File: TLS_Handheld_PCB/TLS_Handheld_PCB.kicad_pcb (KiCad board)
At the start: 4 copper layers, 175 x 100 mm, 95 parts, among them J1 Conn_01x02_Pin, J2 Conn_01x02_Pin, J3 Conn_01x02_Pin, M1 TO-236AB_SOT23_NEX, M2 TO-236AB_SOT23_NEX, U1 LT8640SEV_PBF, U2 LT8640SEV_PBF, U3 LT8619EDD-TRPBF, U4 LAA108STR, U5 SOP65P640X110-14N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

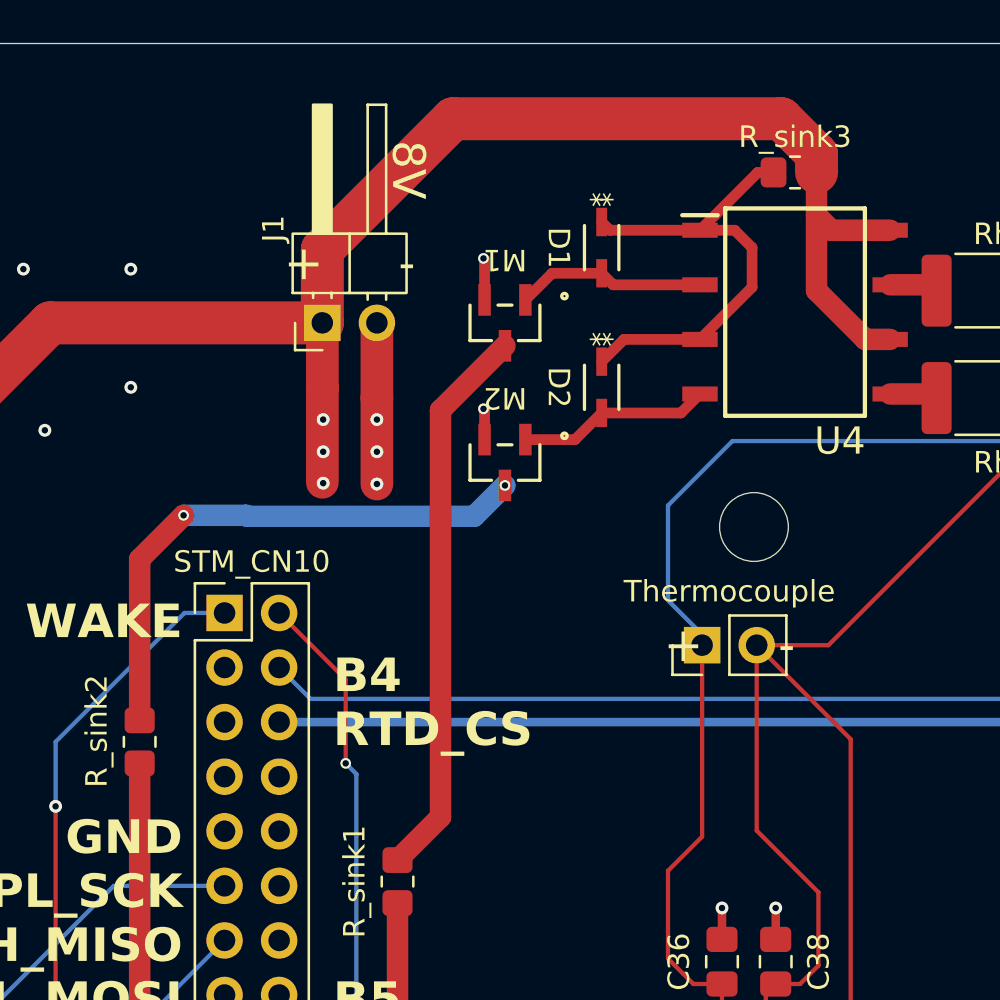
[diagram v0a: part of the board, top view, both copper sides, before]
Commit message: Update relay switching.
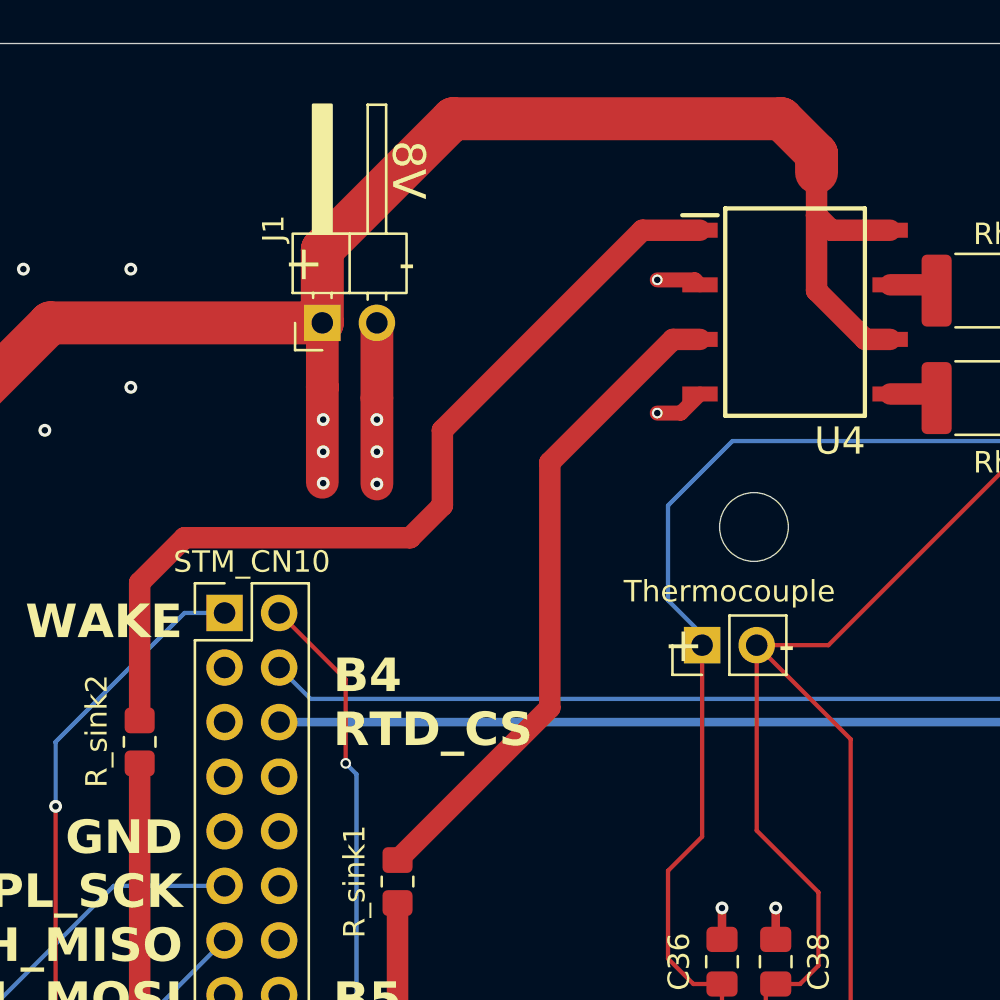
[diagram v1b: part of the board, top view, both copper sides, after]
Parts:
- removed D1, D2: CR_SOD-323_2L_ONS, Library:BAT54HT1G
- removed M1, M2: TO-236AB_SOT23_NEX, Library:2N7002NXAKR
- removed R_sink3: R_0805_2012Metric_Pad1.20x1.40mm_HandSolder, Resistor_SMD:R_0805_2012Metric_Pad1.20x1.40mm_HandSolder
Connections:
- R_sink1 pad 2: MOSFETGait2 -> SW2
- R_sink2 pad 2: MOSFETGait1 -> SW1
- U4 pad 1: SSRin+ -> SW1
- U4 pad 2: SSRin-1 -> GND
- U4 pad 3: SSRin+ -> SW2
- U4 pad 4: SSRin-2 -> GND
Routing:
- net SW1: track 0.00 -> 41.3 mm
- net SW2: track 0.00 -> 30.8 mm
- net MOSFETGait2: track 26.0 -> 0.00 mm
- net MOSFETGait1: track 26.0 -> 0.00 mm, vias 2 -> 0
- net SSRin+: track 22.3 -> 0.00 mm
- net SSRin-2: track 9.00 -> 0.00 mm
- net SSRin-1: track 8.86 -> 0.00 mm
- net GND: track 140.4 -> 141.5 mm

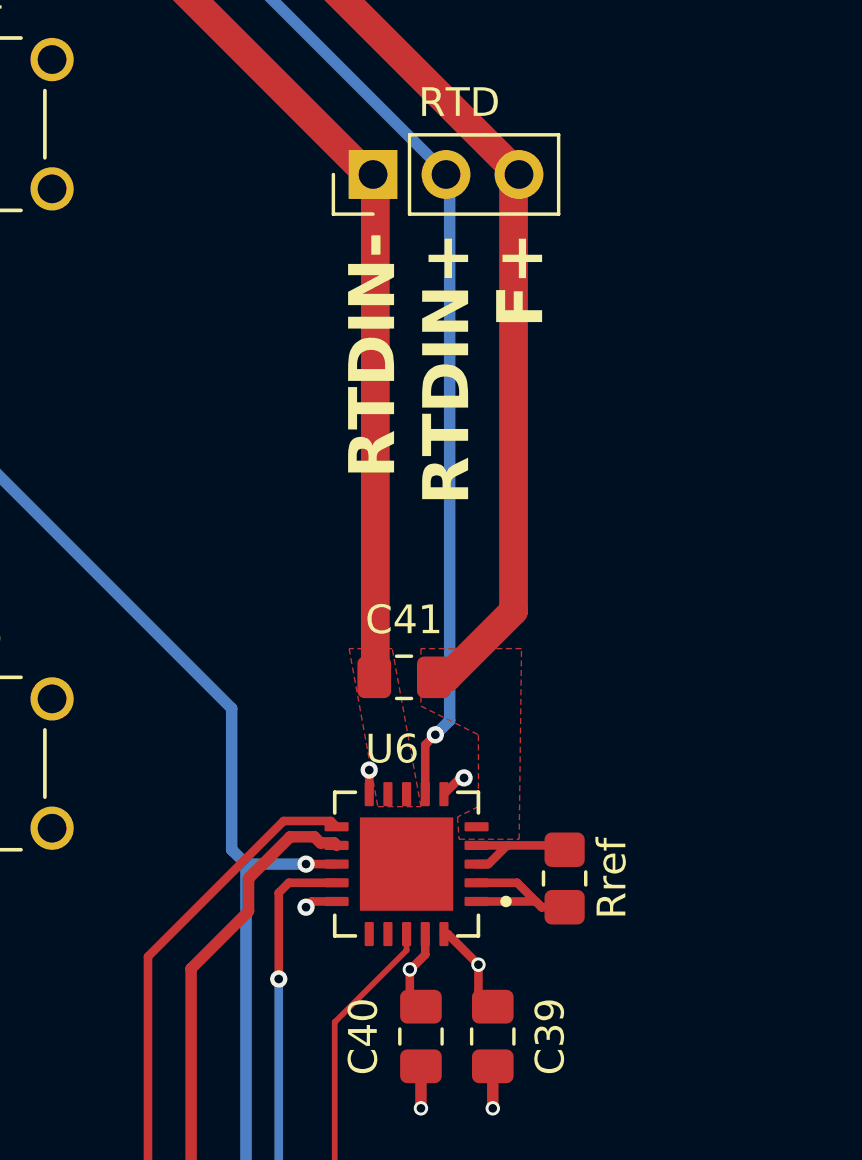
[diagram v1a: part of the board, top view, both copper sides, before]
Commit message: update rtd module wiring.
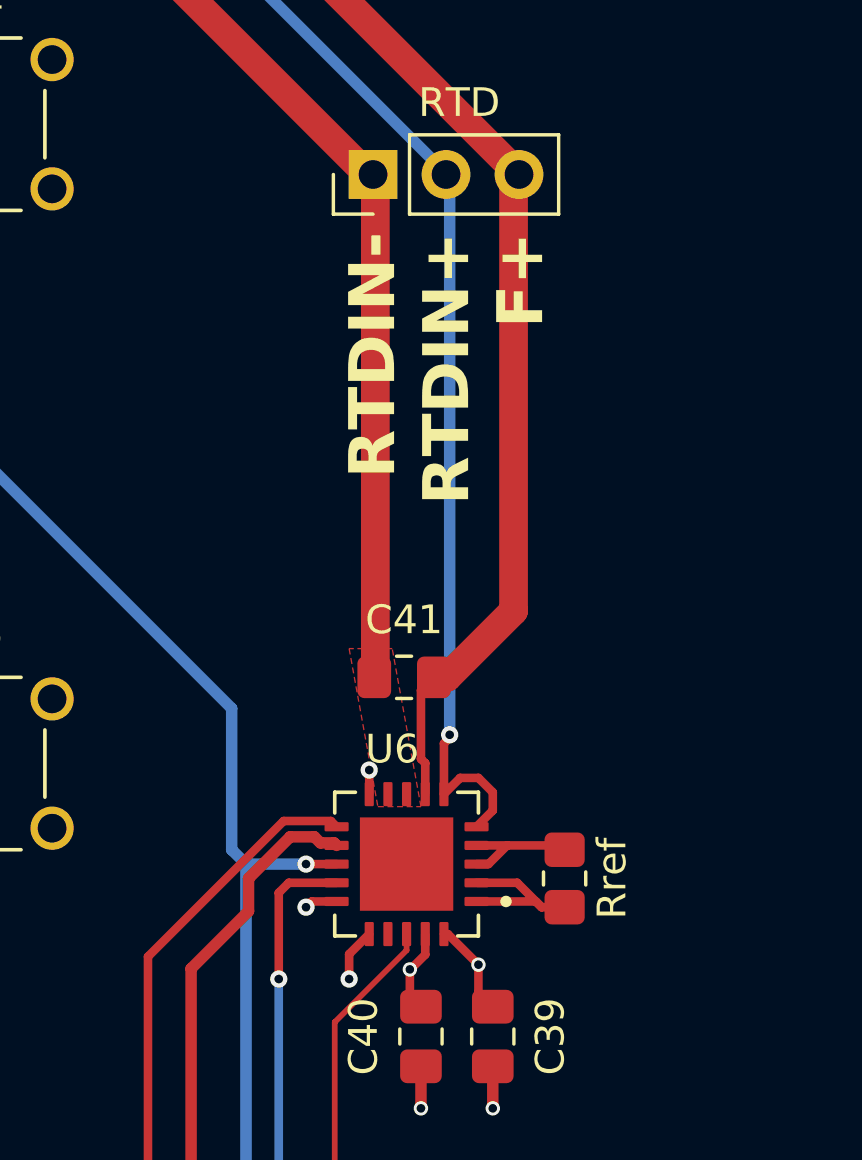
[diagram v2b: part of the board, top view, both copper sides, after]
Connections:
- U6 pad 16: (no net) -> GND
- U6 pad 5: RTD+ -> RTDSens
- U6 pad 6: GND -> RTDSens
- U6 pad 7: RTDSens -> RTD+
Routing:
- net RTD+: track 38.1 -> 42.4 mm
- net RTDSens: track 38.9 -> 42.2 mm
- net GND: track 141.5 -> 142.4 mm
- removed copper zone on F.Cu, net RTD+
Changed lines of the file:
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@@
 			(layers "F.Cu" "F.Mask" "F.Paste")
 			(roundrect_rratio 0.125)
-			(net 31 "RTD+")
+			(net 33 "RTDSens")
 			(solder_mask_margin 0.102)
 		)
@@
 			(layers "F.Cu" "F.Mask" "F.Paste")
 			(roundrect_rratio 0.125)
-			(net 1 "GND")
+			(net 33 "RTDSens")
 			(solder_mask_margin 0.102)
 		)
@@
 			(layers "F.Cu" "F.Mask" "F.Paste")
 			(roundrect_rratio 0.125)
-			(net 33 "RTDSens")
+			(net 31 "RTD+")
 			(solder_mask_margin 0.102)
 		)
@@
 			(layers "F.Cu" "F.Mask" "F.Paste")
 			(roundrect_rratio 0.125)
+			(net 1 "GND")
 			(solder_mask_margin 0.102)
 		)
@@
 	)
 	(segment
+		(start 223.2 94.935)
+		(end 222.5 95.635)
+		(width 0.3)
+		(layer "F.Cu")
+		(net 1)
+	)
+	(segment
 		(start 97.9125 124.5)
 		(end 100.6625 124.5)
@@
 	)
 	(segment
+		(start 222.5 95.635)
+		(end 222.5 96.5)
+		(width 0.3)
+		(layer "F.Cu")
+		(net 1)
+	)
+	(segment
 		(start 140.797 87)
 		(end 141.297 86.5)
@@
 	)
 	(segment
-		(start 226.365 89.5)
-		(end 226.5 89.5)
-		(width 0.3)
-		(layer "F.Cu")
-		(net 1)
-	)
-	(segment
 		(start 133.4195 122.5975)
 		(end 134.4595 121.5575)
@@
 	)
 	(segment
-		(start 225.8 90.065)
-		(end 226.365 89.5)
-		(width 0.3)
-		(layer "F.Cu")
-		(net 1)
-	)
-	(segment
 		(start 128.5 95)
 		(end 128.4266 95.0734)
@@
 	)
 	(via
-		(at 226.5 89.5)
-		(size 0.6)
-		(drill 0.3)
-		(layers "F.Cu" "B.Cu")
-		(net 1)
-	)
-	(via
 		(at 130.709499 55.6978)
 		(size 0.6)
@@
 	)
 	(via
+		(at 222.5 96.5)
+		(size 0.6)
+		(drill 0.3)
+		(layers "F.Cu" "B.Cu")
+		(net 1)
+	)
+	(via
 		(at 132.081242 86.064443)
 		(size 0.6)
@@
 	)
 	(segment
+		(start 225 86.45)
+		(end 225.45 86)
+		(width 0.3)
+		(layer "F.Cu")
+		(net 31)
+	)
+	(segment
+		(start 225.15 88.98781)
+		(end 225 88.83781)
+		(width 0.3)
+		(layer "F.Cu")
+		(net 31)
+	)
+	(segment
 		(start 215.572901 55.660401)
 		(end 228.2225 68.31)
@@
 	)
 	(segment
+		(start 225.15 90.065)
+		(end 225.15 88.98781)
+		(width 0.3)
+		(layer "F.Cu")
+		(net 31)
+	)
+	(segment
+		(start 225 88.83781)
+		(end 225 86.45)
+		(width 0.3)
+		(layer "F.Cu")
+		(net 31)
+	)
+	(segment
 		(start 226.935 92.5)
 		(end 227.35 92.5)
@@
 	)
 	(segment
-		(start 225.5 88)
-		(end 225.15 88.35)
+		(start 226.365 89.5)
+		(end 227 89.5)
 		(width 0.3)
 		(layer "F.Cu")
@@
 	)
 	(segment
-		(start 225.15 88.35)
-		(end 225.15 90.065)
+		(start 227 89.5)
+		(end 227.5 90)
+		(width 0.3)
+		(layer "F.Cu")
+		(net 33)
+	)
+	(segment
+		(start 226 88)
+		(end 226 88.1)
+		(width 0.3)
+		(layer "F.Cu")
+		(net 33)
+	)
+	(segment
+		(start 225.8 90.065)
+		(end 226.365 89.5)
+		(width 0.3)
+		(layer "F.Cu")
+		(net 33)
+	)
+	(segment
+		(start 227.5 90.635)
+		(end 226.935 91.2)
+		(width 0.3)
+		(layer "F.Cu")
+		(net 33)
+	)
+	(segment
+		(start 227.5 90)
+		(end 227.5 90.635)
+		(width 0.3)
+		(layer "F.Cu")
+		(net 33)
+	)
+	(segment
+		(start 225.8 88.3)
+		(end 225.8 90.065)
+		(width 0.3)
+		(layer "F.Cu")
+		(net 33)
+	)
+	(segment
+		(start 226 88.1)
+		(end 225.8 88.3)
 		(width 0.3)
 		(layer "F.Cu")
@@
 	)
 	(via
-		(at 225.5 88)
+		(at 226 88)
 		(size 0.6)
 		(drill 0.3)
@@
 	)
 	(segment
-		(start 225.5 88)
-		(end 226 87.5)
+		(start 226 88)
+		(end 226 68.6275)
 		(width 0.4)
 		(layer "B.Cu")
@@
 	)
 	(segment
-		(start 225.6825 68.27)
-		(end 218.5729 61.1604)
+		(start 225.6825 68.31)
+		(end 225.6825 68.27)
 		(width 0.4)
 		(layer "B.Cu")
@@
 	)
 	(segment
-		(start 225.6825 68.31)
-		(end 225.6825 68.27)
+		(start 225.6825 68.27)
+		(end 218.5729 61.1604)
 		(width 0.4)
 		(layer "B.Cu")
@@
 	)
 	(segment
-		(start 226 87.5)
-		(end 226 68.6275)
-		(width 0.4)
-		(layer "B.Cu")
-		(net 33)
-	)
-	(segment
 		(start 207 53.45)
 		(end 207.05 53.45)
@@
 			)
 		)
-	)
-	(zone
-		(net 31)
-		(net_name "RTD+")
-		(layer "F.Cu")
-		(hatch edge 0.5)
-		(priority 20)
-		(connect_pads yes
-			(clearance 0.5)
-		)
-		(min_thickness 0.25)
-		(filled_areas_thickness no)
-		(fill yes
-			(thermal_gap 0.5)
-			(thermal_bridge_width 0.5)
-		)
-		(polygon
-			(pts
-				(xy 225 85) (xy 225 87) (xy 227 88) (xy 227 90.5) (xy 226.273045 90.860269) (xy 226.327243 91.634524)
-				(xy 228.417733 91.634524) (xy 228.5 85)
-			)
-		)
